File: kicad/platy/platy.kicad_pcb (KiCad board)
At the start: 2 copper layers, 125.8 x 52.6 mm, 87 parts, among them J1 Conn_01x04_Socket, J2 Conn_01x02_Socket, J3 Conn_Coaxial, J5 USB_C_Receptacle_USB2.0_16P, J6 Conn_01x04_Pin, J8 Conn_01x14_Socket, J9 Conn_02x04_Odd_Even, Q4 BC847, Q5 Q_PMOS_GSD, SW1 SW_DPST, SW2 SW_Push(Boot), SW3 SW_Push(EN), U10 ESP32-S3-WROOM-1, U4 CC1101, U5 PN5321A3HN_C1xx, U6 TSOP382xx, U7 AMS1117-3.3, Y2 27.12Mhz, Y3 26MHz

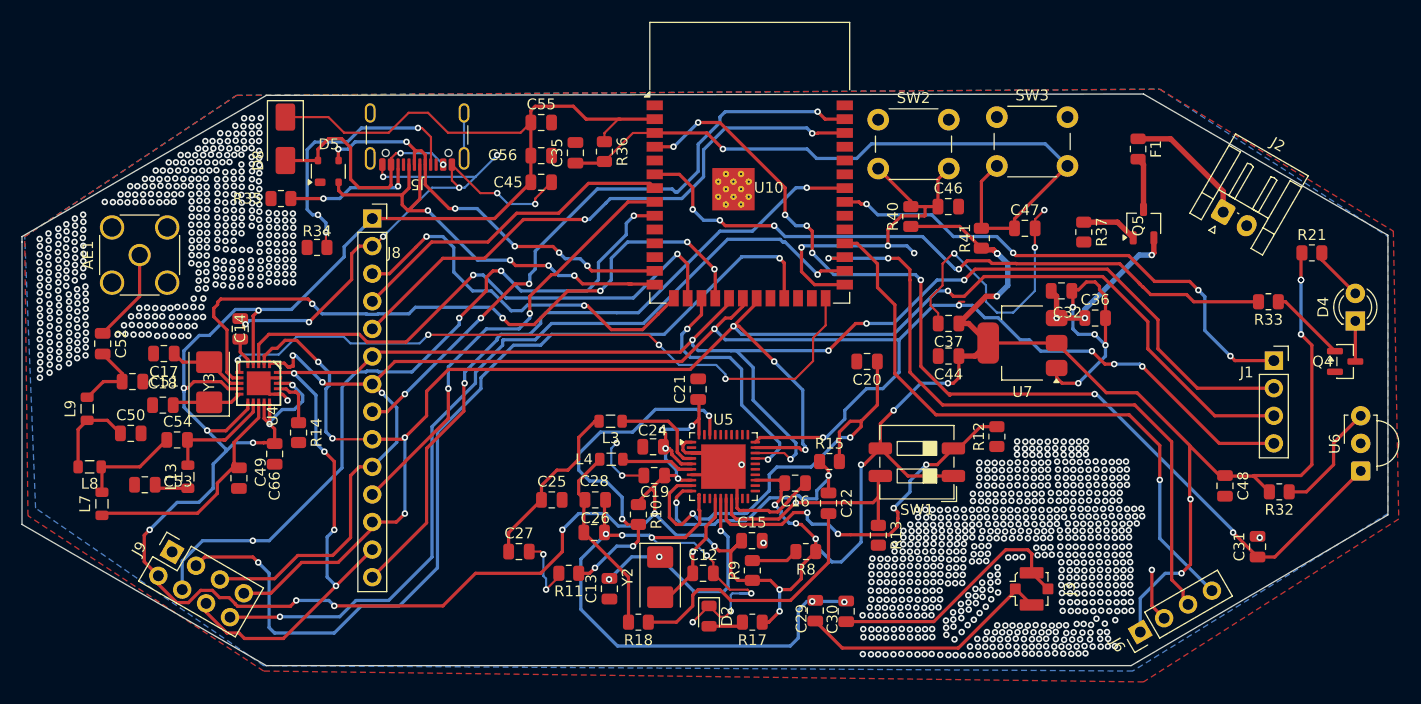
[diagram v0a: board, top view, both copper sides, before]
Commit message: made the changes in the pcb as in the pn532 antenna and added silkscreen
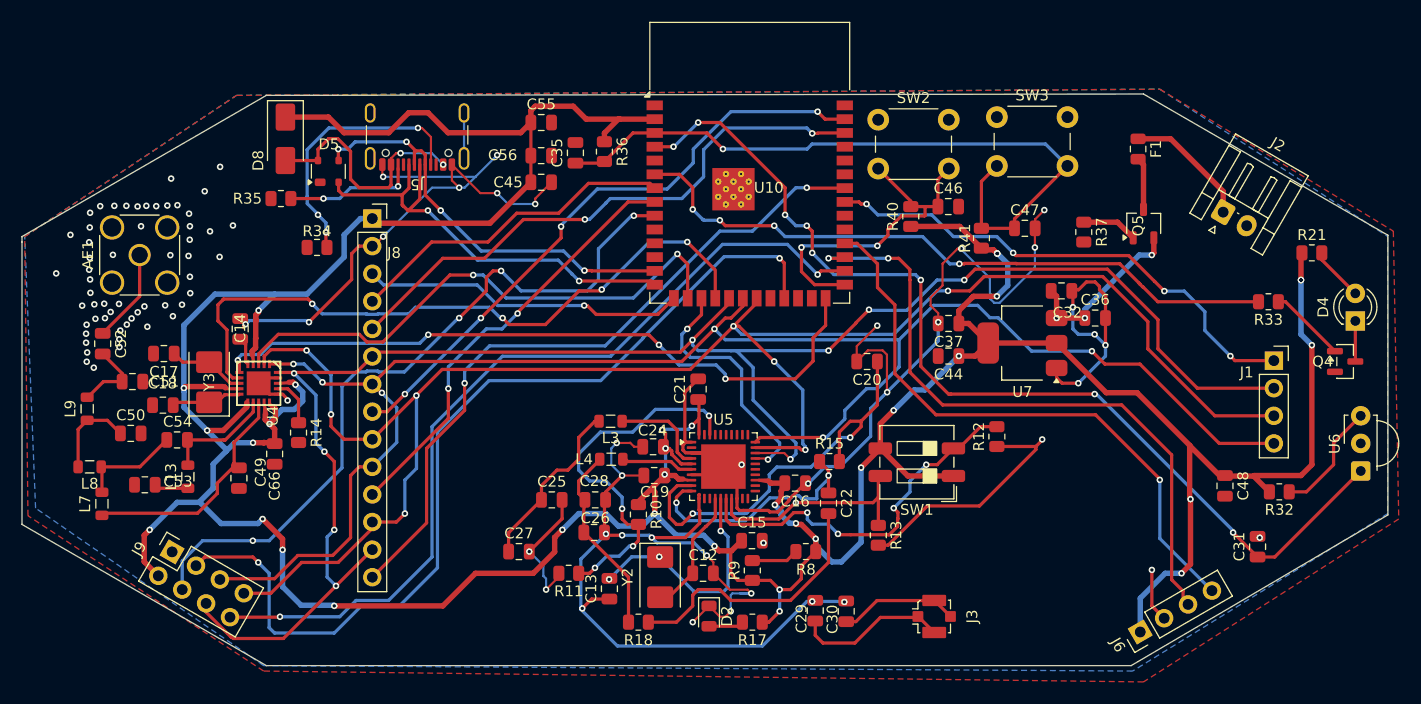
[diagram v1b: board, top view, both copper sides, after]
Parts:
- added G***: LOGO, LOGO, B.Cu at (189.7, 94.6)
- moved J3 9.32 mm to (178.7, 113.0)
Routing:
- net GND: track 282.3 -> 331.4 mm, vias 1122 -> 95
- net /cs_tht: track 35.6 -> 30.2 mm, vias 2 -> 1
- net /3v3: track 406.0 -> 401.7 mm, vias 32 -> 33
- net /BOOT: track 34.9 -> 31.6 mm, vias 3 -> 2
- net /SCK: track 159.8 -> 157.4 mm, vias 9 -> 6
- net /led: track 58.7 -> 56.6 mm
- net /Vry: track 57.0 -> 55.2 mm
- net /CSn: track 63.9 -> 62.2 mm, vias 5 -> 4
- net /MISO: track 164.4 -> 165.8 mm
- net /IRQ: track 80.3 -> 79.1 mm
- net /CSN: track 41.1 -> 40.0 mm
- net /SD_cs: track 47.2 -> 46.4 mm
- net /EN: track 66.2 -> 65.4 mm
- net Net-(U5-RX): track 23.8 -> 23.1 mm
- net /Vrx: track 61.3 -> 60.6 mm
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
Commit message: changes made the in the header configuration
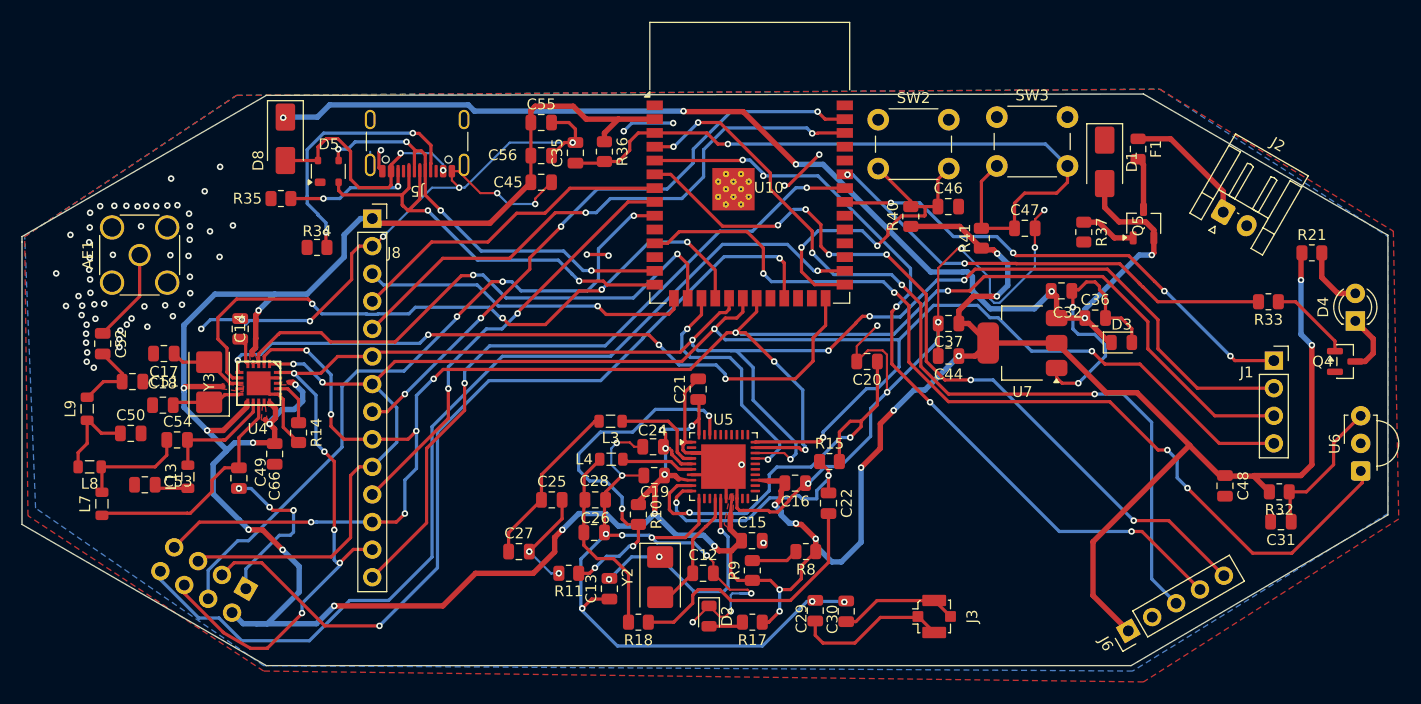
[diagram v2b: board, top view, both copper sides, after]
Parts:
- removed R12, R13: 10K, Resistor_SMD:R_0805_2012Metric
- removed SW1: SW_DPST, Button_Switch_SMD:SW_DIP_SPSTx02_Slide_6.7x6.64mm_W6.73mm_P2.54mm_LowProfile_JPin
- added D1: 1N914, Diode_SMD:D_SMA, F.Cu at (194.4, 71.1)
- added D3: D_Zener, Diode_SMD:D_0805_2012Metric, F.Cu at (196.0, 87.8)
- C44: value 10uF -> 22uF
- J6: value Conn_01x04_Pin -> Conn_01x05_Pin; footprint Connector_PinHeader_2.54mm:PinHeader_1x04_P2.54mm_Vertical -> Connector_PinHeader_2.54mm:PinHeader_1x05_P2.54mm_Vertical
- J9: moved to B.Cu
- moved J9 7.59 mm to (115.4, 110.4)
- moved C31 3.15 mm to (210.7, 104.2), turned to 180 degrees
- moved J6 1.10 mm to (196.6, 114.3)
- moved J5 0.61 mm to (131.1, 68.3)
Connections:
- C31 pad 1: /GPIO 4 -> Net-(U6-Vs)
- D8 pad 1: /3v3 -> /Vin
- R33 pad 2: /gpio 6 -> /gpio 42
- U10 pad 11: unconnected-(U10-IO18-Pad11) -> /GPIO 4
- U10 pad 29: /Vrx -> unconnected-(U10-IO36-Pad29)
- U10 pad 30: /Vry -> unconnected-(U10-IO37-Pad30)
- U10 pad 35: unconnected-(U10-IO42-Pad35) -> /gpio 42
- U10 pad 4: /GPIO 4 -> /Vrx
- U10 pad 5: /IN -> /Vry
- U10 pad 6: /gpio 6 -> /SWITCH
- U5 pad 16: /I0 -> GND
- U5 pad 17: /I1 -> /3v3
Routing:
- net /Vin: track 16.7 -> 108.1 mm, vias 3 -> 6
- net /SWITCH: track 0.00 -> 73.9 mm, vias 0 -> 6
- net /gpio 6: track 61.7 -> 0.00 mm, vias 4 -> 0
- net /gpio 42: track 0.00 -> 42.7 mm, vias 0 -> 2
- net /I0: track 35.2 -> 0.00 mm, vias 4 -> 0
- net /3v3: track 401.7 -> 368.1 mm, vias 33 -> 28
- net /I1: track 20.6 -> 0.00 mm, vias 1 -> 0
- net /Vrx: track 60.6 -> 81.1 mm, vias 2 -> 5
- net /Vry: track 55.2 -> 74.3 mm, vias 1 -> 5
- net /IRQ: track 79.1 -> 89.3 mm, vias 2 -> 1
- net /GPIO 4: track 93.2 -> 87.1 mm, vias 8 -> 4
- net /CE: track 85.5 -> 79.6 mm
- net /CNS: track 67.7 -> 63.0 mm, vias 4 -> 3
- net Net-(U6-Vs): track 10.7 -> 13.6 mm
- net /MISO: track 165.8 -> 167.9 mm, vias 8 -> 10
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- added copper zone on F.Cu, net /3v3

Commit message: changes the naming mismatched and the some pin connnection also
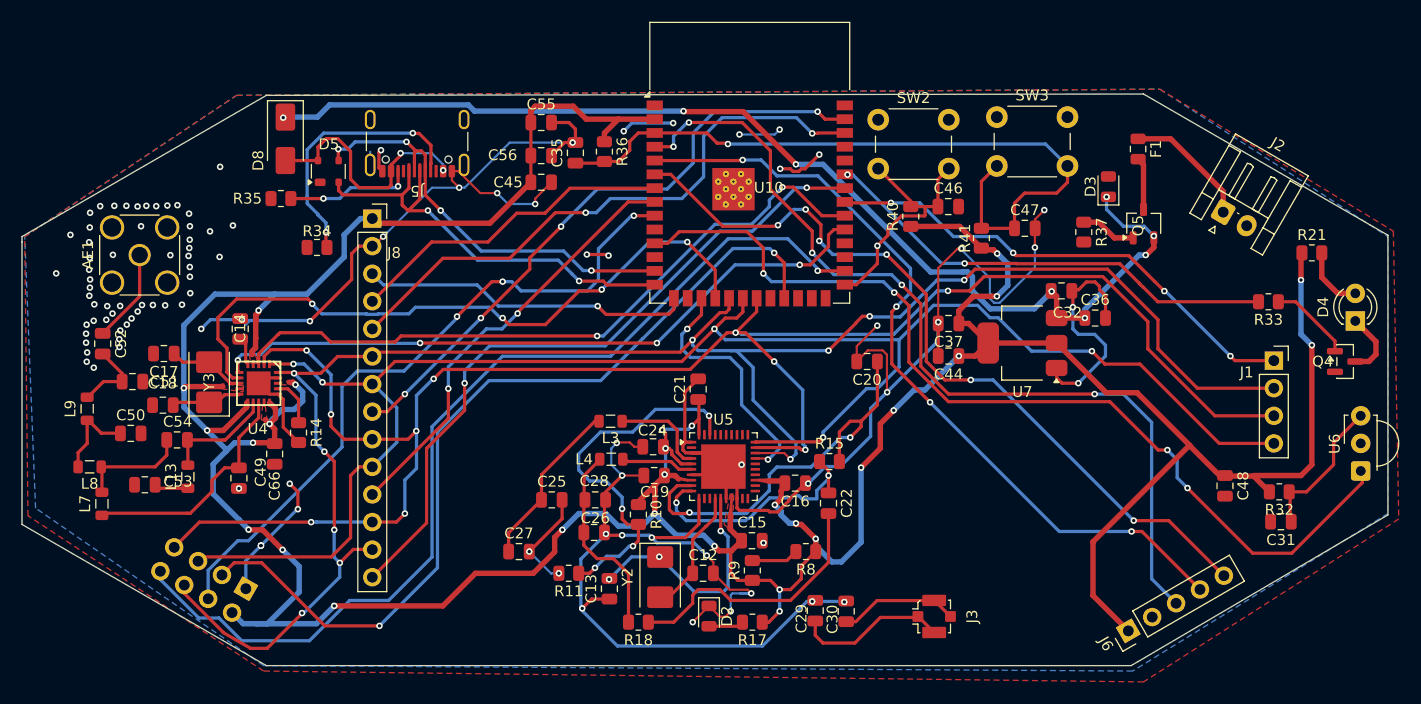
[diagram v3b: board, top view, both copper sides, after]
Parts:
- removed D1: 1N914, Diode_SMD:D_SMA
- moved D3 14.4 mm to (194.8, 73.4), turned to 90 degrees
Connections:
- net /GPIO 4 renamed /GPIO 18
- U10 pad 10: /LCD_DC -> unconnected-(U10-IO17-Pad10)
- U10 pad 12: /LCD_RST -> unconnected-(U10-IO8-Pad12)
- U10 pad 16: /gdo2 -> unconnected-(U10-IO46-Pad16)
- U10 pad 22: /LCD_CS -> unconnected-(U10-IO14-Pad22)
- U10 pad 24: /GPIO 47 -> unconnected-(U10-IO47-Pad24)
- U10 pad 25: /GPIO 48 -> unconnected-(U10-IO48-Pad25)
- U10 pad 26: /GDO0 -> unconnected-(U10-IO45-Pad26)
- U10 pad 31: /GPIO 38 -> /GDO0
- U10 pad 32: /OUT -> /gdo2
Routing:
- net /gdo2: track 50.2 -> 63.4 mm
- net /BOOT: track 32.8 -> 23.3 mm, vias 2 -> 1
- net /Vin: track 108.1 -> 102.7 mm, vias 6 -> 8
- net GND: track 331.7 -> 328.0 mm, vias 98 -> 102
- net /Vrx: track 81.1 -> 82.9 mm
- net /d/c: track 52.9 -> 54.4 mm
- net /GDO0: track 64.1 -> 62.6 mm
- net /led: track 56.6 -> 57.5 mm
- net /CE: track 79.6 -> 80.4 mm
- net /IRQ: track 89.3 -> 89.8 mm
- net /Vry: track 74.3 -> 74.1 mm, vias 5 -> 4

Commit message: made the changes in the pcb as previous diode was there and changes the name also some issue
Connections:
- D3 pad 2: GND -> Net-(D3-A)
- Q5 pad 1: Net-(Q5-G) -> Net-(D3-A)
- R37 pad 1: Net-(Q5-G) -> Net-(D3-A)
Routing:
- net Net-(D3-A): track 0.00 -> 11.1 mm
- net Net-(Q5-G): track 5.15 -> 0.00 mm
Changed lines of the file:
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@@
 			(layers "F.Cu" "F.Mask" "F.Paste")
 			(roundrect_rratio 0.25)
-			(net "GND")
+			(net "Net-(D3-A)")
 			(pinfunction "A_2")
 			(pintype "passive")
@@
 			(layers "F.Cu" "F.Mask" "F.Paste")
 			(roundrect_rratio 0.243902)
-			(net "Net-(Q5-G)")
+			(net "Net-(D3-A)")
 			(pintype "passive")
 		)
@@
 			(layers "F.Cu" "F.Mask" "F.Paste")
 			(roundrect_rratio 0.25)
-			(net "Net-(Q5-G)")
+			(net "Net-(D3-A)")
 			(pinfunction "G_1")
 			(pintype "input")
@@
 		(width 0.5)
 		(layer "F.Cu")
-		(net "Net-(Q5-G)")
+		(net "Net-(D3-A)")
 	)
 	(segment
@@
 		(width 0.5)
 		(layer "F.Cu")
-		(net "Net-(Q5-G)")
+		(net "Net-(D3-A)")
+	)
+	(segment
+		(start 192.5 73.3)
+		(end 192.5 76.675)
+		(width 0.3)
+		(layer "F.Cu")
+		(net "Net-(D3-A)")
+	)
+	(segment
+		(start 193.3325 72.4675)
+		(end 192.5 73.3)
+		(width 0.3)
+		(layer "F.Cu")
+		(net "Net-(D3-A)")
+	)
+	(segment
+		(start 194.77 72.4675)
+		(end 193.3325 72.4675)
+		(width 0.3)
+		(layer "F.Cu")
+		(net "Net-(D3-A)")
 	)
 	(segment
@@
 		(width 0.5)
 		(layer "F.Cu")
-		(net "Net-(Q5-G)")
+		(net "Net-(D3-A)")
 	)
 	(zone

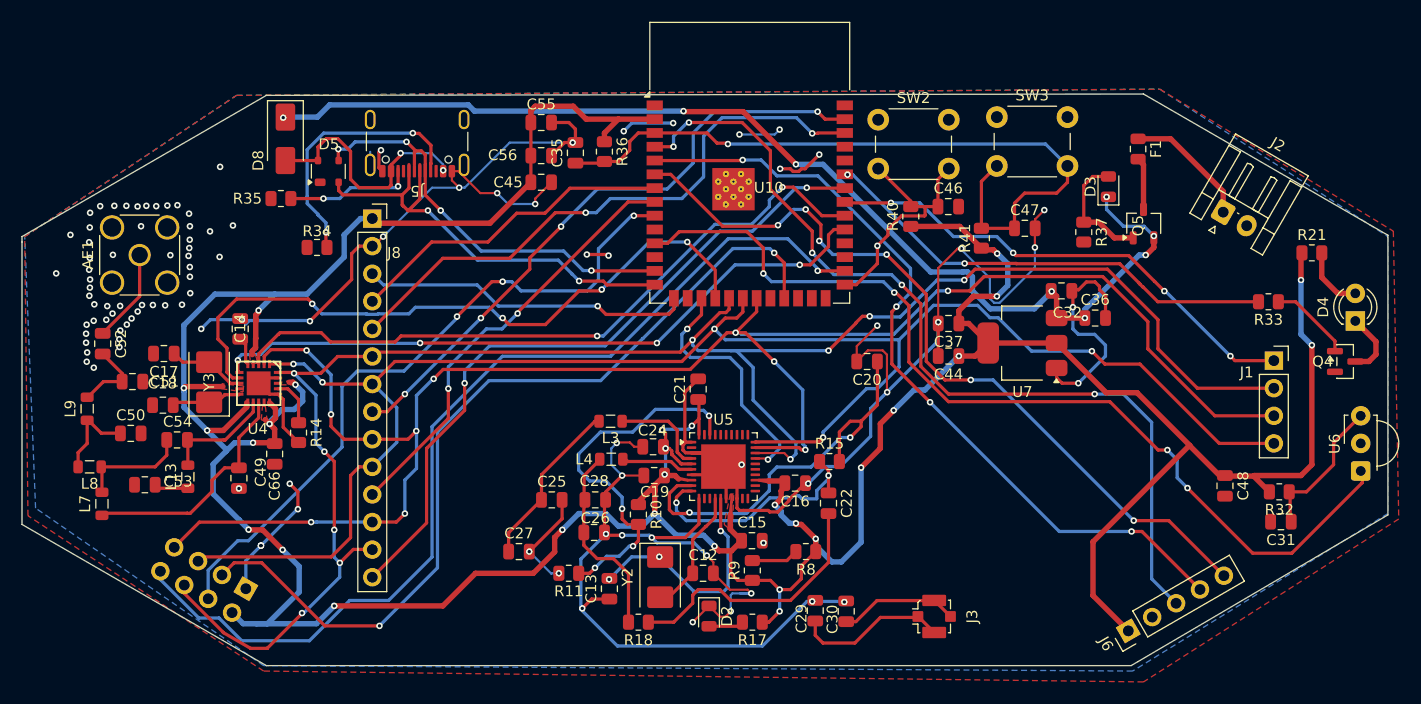
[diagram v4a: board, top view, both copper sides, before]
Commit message: changes made in the impedance of the antenna and the make the circuit of the aligned straight
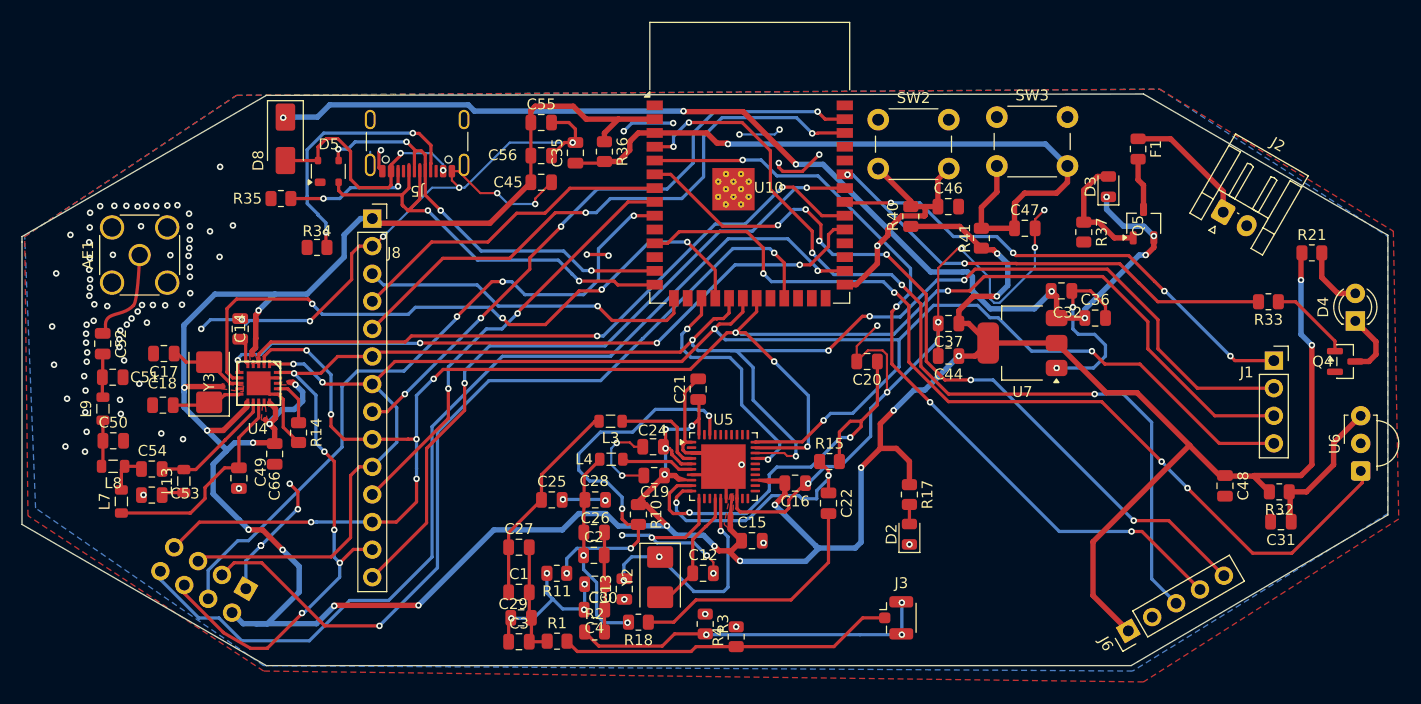
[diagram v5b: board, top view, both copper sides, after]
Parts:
- removed R8, R9: 4.7K, Resistor_SMD:R_0805_2012Metric
- added C1: NC, Capacitor_SMD:C_0805_2012Metric, F.Cu at (140.5, 110.8)
- added C2: NC, Capacitor_SMD:C_0805_2012Metric, F.Cu at (147.4, 107.3)
- added C3: NC, Capacitor_SMD:C_0805_2012Metric, F.Cu at (140.5, 115.3)
- added C4: NC, Capacitor_SMD:C_0805_2012Metric, F.Cu at (147.4, 112.3)
- added R1: 1.5, Resistor_SMD:R_0805_2012Metric, F.Cu at (144.0, 115.2)
- added R2: 1.5, Resistor_SMD:R_0805_2012Metric, F.Cu at (147.5, 114.4)
- added R3: NC, Resistor_SMD:R_0805_2012Metric, F.Cu at (157.7, 113.7)
- added R4: NC, Resistor_SMD:R_0805_2012Metric, F.Cu at (160.5, 114.8)
- J3: footprint Connector_Coaxial:U.FL_Molex_MCRF_73412-0110_Vertical -> Connector_Coaxial:U.FL_Hirose_U.FL-R-SMT-1_Vertical
- R14: value R -> 56k
- moved C29 27.1 mm to (140.7, 113.1), turned to 0 degrees
- moved C30 23.3 mm to (147.5, 110.0), turned to 180 degrees
- moved D2 19.9 mm to (176.4, 105.4), turned to 90 degrees
- moved R17 18.6 mm to (176.4, 101.8), turned to -90 degrees
- moved C54 3.55 mm to (106.7, 99.4)
- moved J3 3.03 mm to (175.7, 113.1), turned to 0 degrees
- moved L8 2.16 mm to (103.1, 99.2)
- moved C51 1.86 mm to (103.1, 91.0)
- moved L7 1.80 mm to (103.9, 102.4)
- moved C50 1.75 mm to (103.2, 96.8)
- moved L9 1.45 mm to (102.2, 93.8)
- moved C13 1.37 mm to (150.2, 110.5)
- moved C53 1.15 mm to (106.7, 101.8)
- moved R11 1.10 mm to (144.0, 109.0)
- moved L13 0.55 mm to (109.7, 100.5)
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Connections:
- C27 pad 2: GND -> Net-(C1-Pad2)
- C28 pad 2: GND -> Net-(C2-Pad2)
- C29 pad 2: GND -> Net-(C1-Pad2)
- C30 pad 1: GND -> Net-(C2-Pad2)
- J3 pad 1: GND -> Net-(J3-In)
- J3 pad 2: GND -> Net-(J3-Ext)
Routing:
- net GND: track 328.0 -> 251.0 mm, vias 102 -> 117
- net Net-(J3-Ext): track 0.00 -> 33.1 mm, vias 0 -> 3
- net Net-(J3-In): track 0.00 -> 30.9 mm
- net Net-(C1-Pad2): track 0.00 -> 10.5 mm
- net Net-(C2-Pad2): track 0.00 -> 9.24 mm
- net Net-(AE1-A): track 8.62 -> 0.00 mm
- net /3v3: track 368.1 -> 360.6 mm, vias 28 -> 25
- net Net-(C54-Pad1): track 10.2 -> 3.95 mm
- net /SSEL/SCL/RX: track 4.36 -> 0.00 mm
- net Net-(C50-Pad1): track 8.19 -> 4.29 mm
- net Net-(C1-Pad1): track 15.7 -> 19.4 mm
- net Net-(C51-Pad1): track 7.04 -> 4.01 mm
- net /RSTPD_N: track 34.2 -> 36.1 mm
- net Net-(U4-RF_P): track 10.3 -> 11.9 mm
- net Net-(U4-RF_N): track 21.5 -> 19.9 mm
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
